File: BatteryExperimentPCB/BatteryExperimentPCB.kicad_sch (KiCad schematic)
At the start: 32 parts, among them J1 TYPE-C-31-M-12, J2 Conn_01x12_Pin, J3 Conn_01x12_Pin, Q1 DMG1012T, SW1 SW_Push, U1 ATtiny3226-M, U2 USBLC6-2P6, U3 BQ25628RYKR

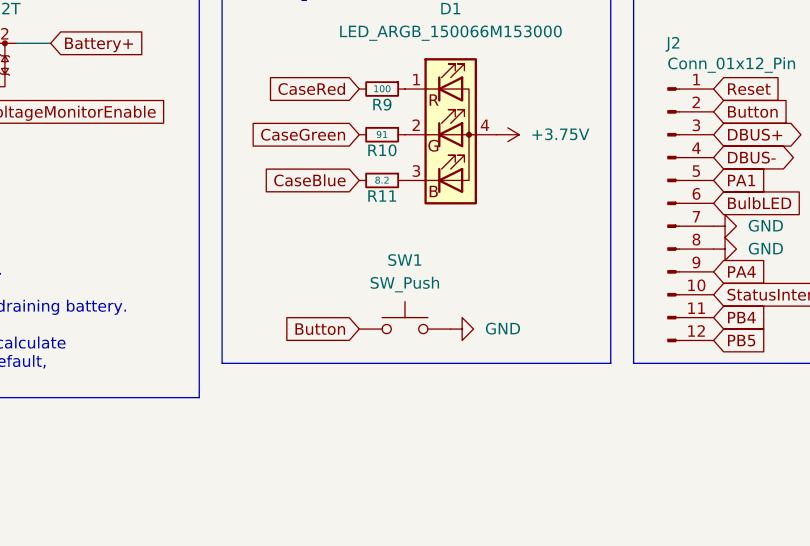
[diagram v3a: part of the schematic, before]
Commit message: replaced button footprint with one from jlcpcb, moved usb c over to the right to fit button
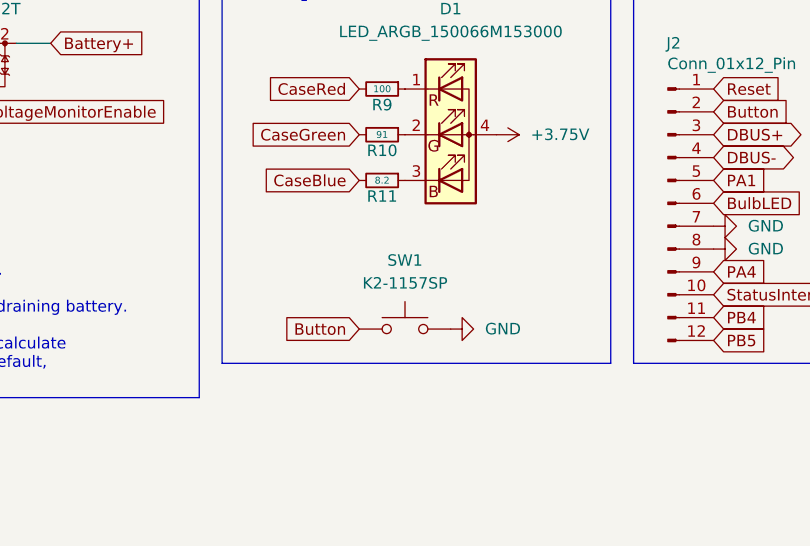
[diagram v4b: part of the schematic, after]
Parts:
- SW1: value SW_Push -> K2-1157SP; footprint Resistor_SMD:R_0603_1608Metric -> BatteryExperimentPCB:K2-1157SP
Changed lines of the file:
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@@
 			)
 		)
-		(property "Value" "SW_Push"
+		(property "Value" "K2-1157SP"
 			(at 176.53 115.57 0)
 			(effects
@@
 			)
 		)
-		(property "Footprint" "Resistor_SMD:R_0603_1608Metric"
+		(property "Footprint" "BatteryExperimentPCB:K2-1157SP"
 			(at 176.53 115.57 0)
 			(effects
@@
 			)
 		)
-		(property "Datasheet" "~"
+		(property "Datasheet" "https://jlcpcb.com/partdetail/3187750-K2_1157SP_I4SW01/C2909692"
 			(at 176.53 115.57 0)
 			(effects

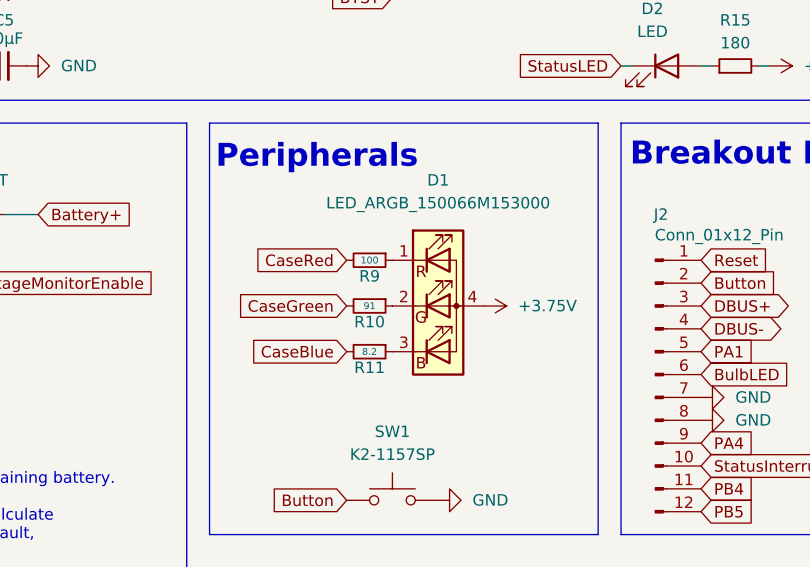
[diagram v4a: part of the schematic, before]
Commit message: changed led to one with common cathode
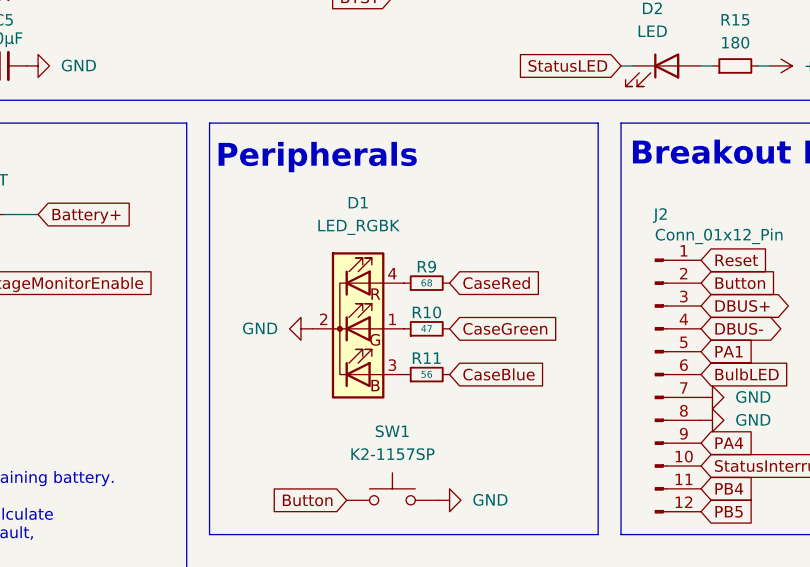
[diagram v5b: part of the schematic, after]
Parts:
- removed D1: LED_ARGB_150066M153000, BatteryExperimentPCB:150066M153000, symbol BatteryExperimentPCB:LED_ARGB_150066M153000
- added D1: LED_RGBK, BatteryExperimentPCB:RS-C1415MBAR, symbol BatteryExperimentPCB:LED_RGBK
- R10: value 91 -> 47
- R11: value 8.2 -> 56
- R9: value 100 -> 68
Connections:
- net GND: now also D1.2 (K)
- net at R11.1: now also D1.3 (BA)
- net at R9.1: now also D1.4 (RA)
- net at R10.1: now also D1.1 (GA)
